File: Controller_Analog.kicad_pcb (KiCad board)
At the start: 2 copper layers, 31 parts, among them J1 AnalogIO, J2 Switch_Control, J3 Conn_01x02, SW1 SW_SPDT, SW2 SW_SPDT, SW3 SW_SPDT, SW4 SW_SPDT, U1 S-89713B-K8T2U, U2 S-89713B-K8T2U, U4 NJM2825F

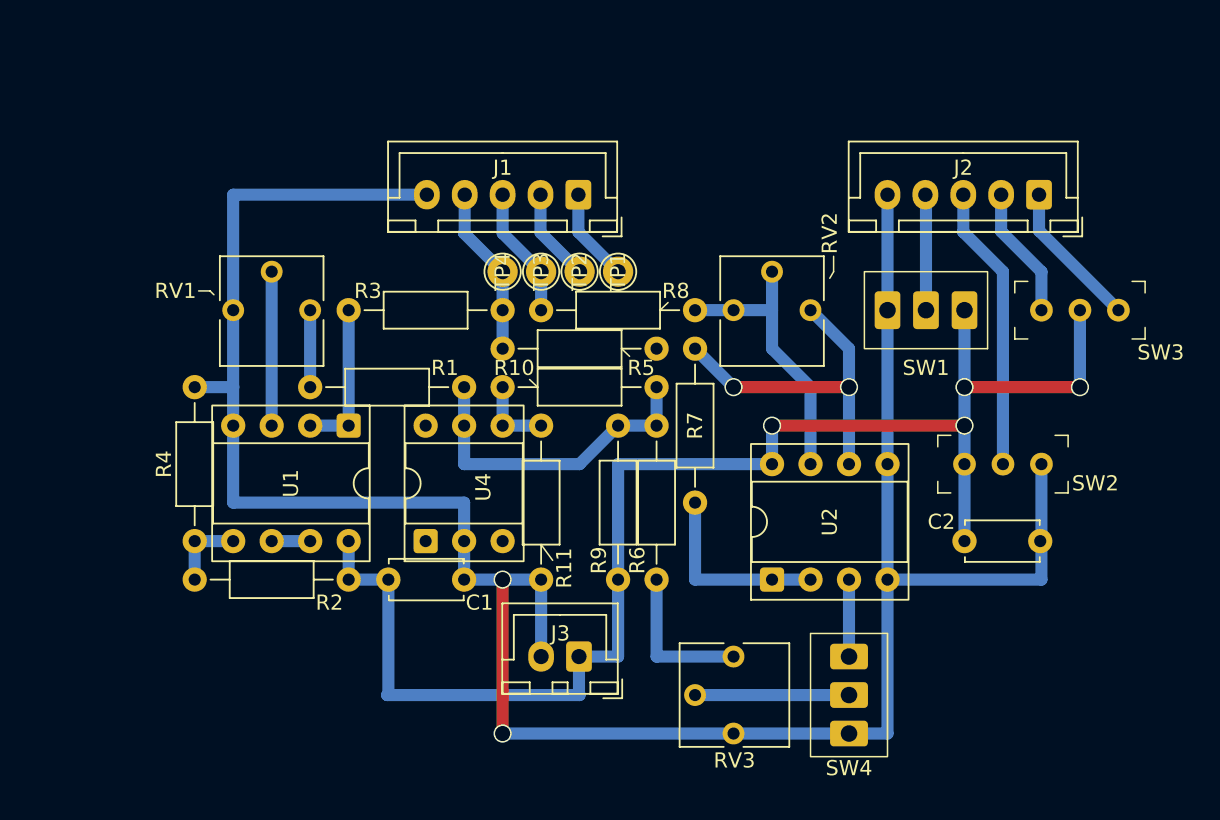
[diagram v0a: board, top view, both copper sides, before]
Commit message: wired components
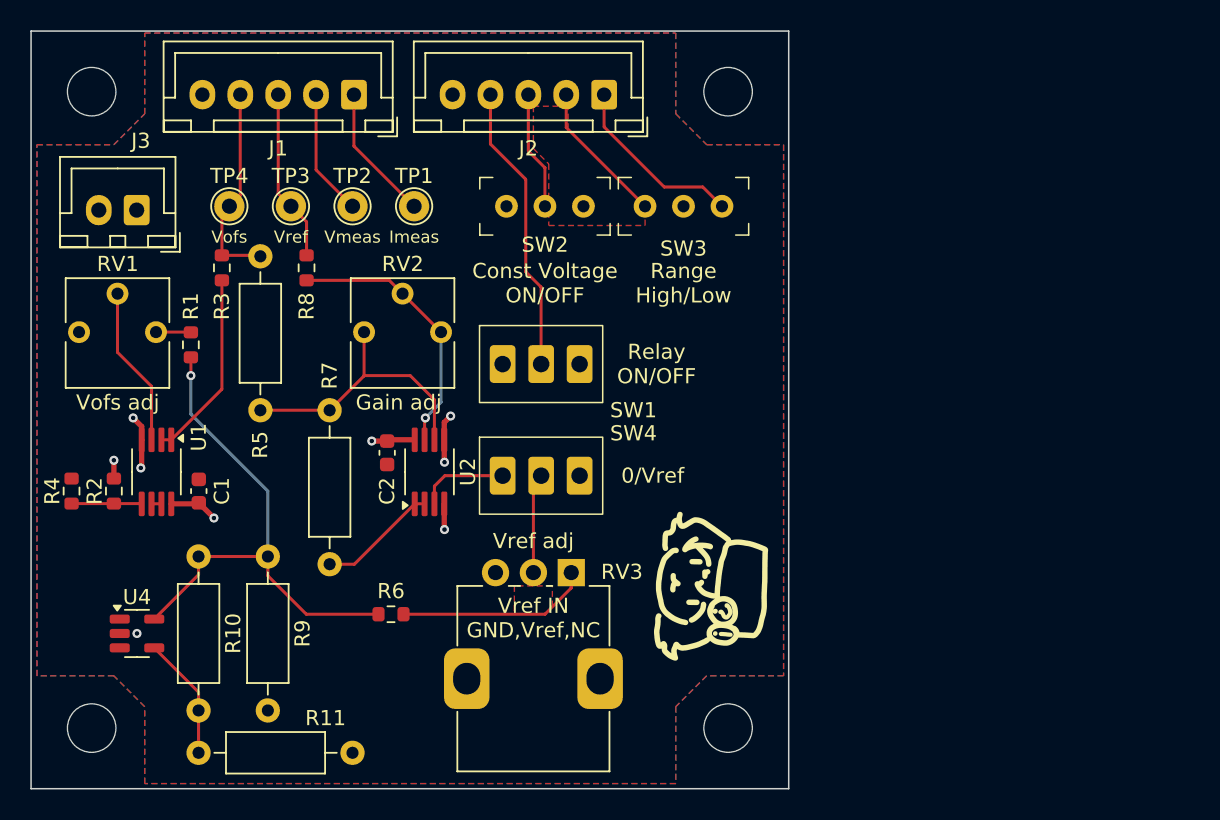
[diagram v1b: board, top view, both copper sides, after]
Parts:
- removed REF**: UniversalC_72x47, AM_Universal:UniversalC_72x47
- added H1: MountingHole, MountingHole:MountingHole_3.2mm_M3, F.Cu at (44.0, 44.0)
- added H2: MountingHole, MountingHole:MountingHole_3.2mm_M3, F.Cu at (86.0, 44.0)
- added H3: MountingHole, MountingHole:MountingHole_3.2mm_M3, F.Cu at (86.0, 86.0)
- added H4: MountingHole, MountingHole:MountingHole_3.2mm_M3, F.Cu at (44.0, 86.0)
- added P1: Eoshi-chan_Silk, Eoshi-chan_v2:Eoshi-chan-v2_10x10, F.Cu at (84.8, 76.7)
- C1, C2: footprint Capacitor_THT:C_Disc_D4.7mm_W2.5mm_P5.00mm -> Capacitor_SMD:C_0603_1608Metric
- R1, R2, R3, R4, R6, R8: footprint Inductor_THT:L_Axial_L5.3mm_D2.2mm_P10.16mm_Horizontal_Vishay_IM-1 -> Resistor_SMD:R_0603_1608Metric
- R10, R11, R5, R7, R9: footprint Inductor_THT:L_Axial_L5.3mm_D2.2mm_P10.16mm_Horizontal_Vishay_IM-1 -> Resistor_THT:R_Axial_DIN0207_L6.3mm_D2.5mm_P10.16mm_Horizontal
- RV3: footprint Potentiometer_THT:Potentiometer_Vishay_T73YP_Vertical -> Potentiometer_THT:Potentiometer_Alps_RK09K_Single_Vertical
- U1, U2: footprint Package_DIP:DIP-8_W7.62mm_Socket -> Package_SO:MSOP-8_3x3mm_P0.65mm
- U4: footprint Package_DIP:DIP-6_W7.62mm_Socket -> Package_TO_SOT_SMD:SOT-23-5
- moved J3 41.5 mm to (47.0, 51.8)
- moved C2 38.5 mm to (63.5, 67.8), turned to -90 degrees
- moved SW2 34.7 mm to (73.9, 51.6), turned to 180 degrees
- moved J2 29.5 mm to (77.8, 44.2)
- moved R10 29.3 mm to (51.1, 84.8), turned to 90 degrees
- moved SW3 27.0 mm to (83.1, 51.6)
- moved R5 26.5 mm to (55.1, 65.0), turned to 90 degrees
- moved R8 25.8 mm to (58.2, 55.6), turned to 90 degrees
- moved SW1 25.6 mm to (73.7, 62.0), turned to 0 degrees
- moved SW4 25.0 mm to (73.7, 69.3), turned to 0 degrees
- moved R9 24.7 mm to (55.6, 74.7)
- moved R7 24.5 mm to (59.7, 65.0)
- moved RV2 24.4 mm to (67.1, 59.9)
- moved U2 23.7 mm to (66.3, 69.1)
- moved U4 20.0 mm to (47.0, 79.8), turned to 0 degrees
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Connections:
- RV2 pad 1: Net-(R5-Pad1) -> Net-(R8-Pad1)
- RV2 pad 3: Net-(R8-Pad1) -> Net-(R5-Pad1)
- SW1 pad 1: +5V -> GND
- SW1 pad 3: GND -> +5V
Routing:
- net GND: track 155.0 -> 8.49 mm, vias 2 -> 6
- net +5V: track 96.7 -> 7.34 mm, vias 4 -> 3
- net VAA: track 21.4 -> 34.8 mm, vias 0 -> 1
- net LOAD_ENABLE: track 7.64 -> 19.2 mm
- net Vconst_ENABLE: track 18.9 -> 7.82 mm
- net Net-(R7-Pad2): track 12.7 -> 7.91 mm
- net Net-(R5-Pad1): track 22.4 -> 18.6 mm, vias 2 -> 0
- net Net-(SW4-B): track 10.2 -> 6.52 mm
- net Net-(U4-FB): track 5.08 -> 8.14 mm
- net Imeas: track 6.17 -> 9.01 mm
- net Net-(R1-Pad1): track 5.08 -> 2.31 mm
- net Vref: track 8.67 -> 11.4 mm
- net Net-(R6-Pad1): track 10.2 -> 12.8 mm
- net Vofs: track 11.2 -> 13.7 mm
- net Net-(R3-Pad1): track 10.2 -> 12.6 mm
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- added copper zone on In2.Cu, net +5V
- added copper zone on B.Cu, net GND
- added copper zone on F.Cu, net GND
- added copper zone on In1.Cu, net GND
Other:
- board outline added: 50 x 50 mm
- copper layers 2 -> 4
- board text added: "0/Vref"
- board text added: "Const Voltage ON/OFF"
- board text added: "Gain adj"
- board text added: "Imeas"
- board text added: "Range High/Low"
- board text added: "Relay ON/OFF"
- board text added: "Vmeas"
- board text added: "Vofs"
- board text added: "Vofs adj"
- board text added: "Vref"
- board text added: "Vref IN GND,Vref,NC"
- board text added: "Vref adj"
